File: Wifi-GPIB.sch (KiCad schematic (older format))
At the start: 18 parts

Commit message: Started dividing subsheets and sorted out power circuits. Active switching on USB/DC connector 5V.
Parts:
- removed CON?: POWER_BARREL, symbol BARREL_JACK
- removed U?: MICRO-B_USB, symbol MICRO-B_USB
- removed U?: BA33BC0FP-E2, TO-252, symbol BA33BC0FP-E2
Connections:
- wire segments 18 -> 19
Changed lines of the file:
@@
 LIBS:esp8266
 LIBS:ba33bc0fp-e2
+LIBS:ap1117e50g-13
+LIBS:irlml2246tr
 LIBS:Wifi-GPIB-cache
 EELAYER 25 0
@@
 $Descr A4 11693 8268
 encoding utf-8
-Sheet 1 1
+Sheet 1 2
 Title ""
 Date ""
@@
 $EndComp
 $Comp
-L BARREL_JACK CON?
-U 1 1 5564DEB5
-P 1250 1000
-F 0 "CON?" H 1250 1250 60  0000 C CNN
-F 1 "POWER_BARREL" H 1250 800 60  0000 C CNN
-F 2 "" H 1250 1000 60  0000 C CNN
-F 3 "" H 1250 1000 60  0000 C CNN
-	1    1250 1000
-	1    0    0    -1
-$EndComp
-$Comp
-L MICRO-B_USB U?
-U 1 1 5564E0EA
-P 1250 1900
-F 0 "U?" H 1250 1600 50  0000 C CNN
-F 1 "MICRO-B_USB" H 1250 2200 50  0000 C CNN
-F 2 "" H 1250 1900 60  0000 C CNN
-F 3 "" H 1250 1900 60  0000 C CNN
-	1    1250 1900
-	1    0    0    -1
-$EndComp
-$Comp
 L ESP-12/07v2/08v2 U?
 U 1 1 5564D82B
@@
 F 3 "" H 7850 1650 60  0000 C CNN
 	1    7850 1650
-	1    0    0    -1
-$EndComp
-$Comp
-L BA33BC0FP-E2 U?
-U 1 1 5564E643
-P 2850 950
-F 0 "U?" H 2650 1150 40  0000 C CNN
-F 1 "BA33BC0FP-E2" H 2850 1150 40  0000 L CNN
-F 2 "TO-252" H 2850 1050 30  0000 C CIN
-F 3 "" H 2850 950 60  0000 C CNN
-	1    2850 950
 	1    0    0    -1
 $EndComp
@@
 	10150 1850 10150 1900
 Wire Wire Line
-	9950 2400 10400 2400
+	9950 2400 10150 2400
+Wire Wire Line
+	10150 2400 10400 2400
 Wire Wire Line
 	11000 2400 11000 2550
@@
 Text GLabel 9050 1400 2    39   Input ~ 0
 ESP_TX
+$Sheet
+S 5100 7050 1700 600
+U 5565FD51
+F0 "Power Circuitry" 60
+F1 "power.sch" 60
+$EndSheet
 $EndSCHEMATC

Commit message: Update main sch to reference heirarchy. Add some more stuff to ESP.
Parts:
- removed D?: LED_DATA, symbol LED
- removed D?: LED_POWER, symbol LED
- removed JP?: ESP_FLASH_JUMP, symbol JUMPER
- removed P?: CONN_CENTRONICS_24, symbol CONN_CENTRONICS_24
- removed P?: CONN_4, symbol CONN_4
- removed R?: R, symbol R
- removed SW?: SW_RESET, symbol SW_PUSH
- removed U?: STM32F030C6, LQFP48, symbol STM32F030C6
- removed U?: SN75160B, MODULE, symbol SN75160B
- removed U?: SN75162B, MODULE, symbol SN75162B
- removed U?: ESP-12/07v2/08v2, symbol ESP-12/07v2/08v2
- removed W? (x2): TEST_GND, symbol TEST
- removed W?: TEST_3.3, symbol TEST
- removed W?: TEST_VIN, symbol TEST
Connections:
- net labels removed: +3.3V, ESP_GPIO0, ESP_RX, ESP_TX, GND, RESET
- wire segments 19 -> 0
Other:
- note removed: "ESP8266 Wifi Module"

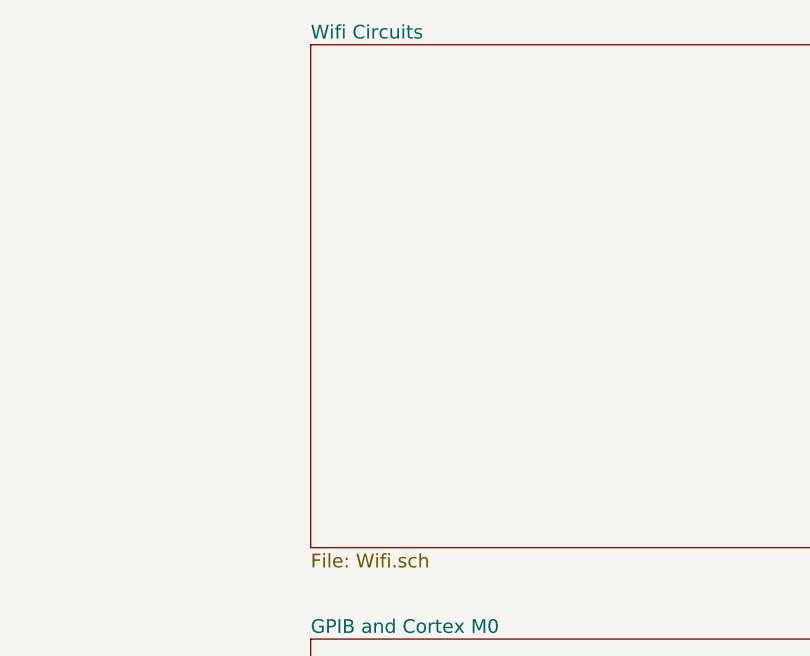
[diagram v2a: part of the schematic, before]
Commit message: Add testpoints and tidy up
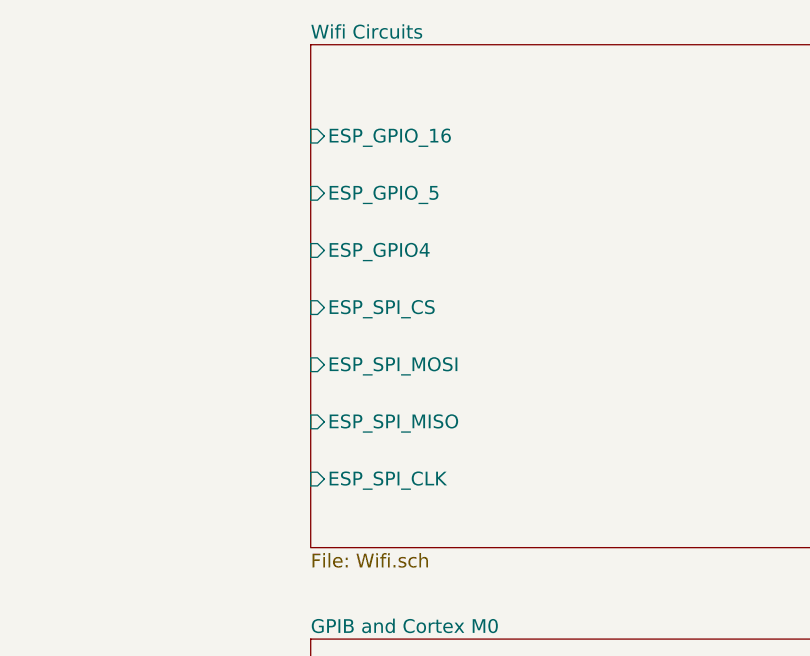
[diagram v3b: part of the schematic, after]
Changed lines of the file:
@@
 LIBS:ap1117e50g-13
 LIBS:irlml2246tr
+LIBS:testpoint
 LIBS:Wifi-GPIB-cache
 EELAYER 25 0
@@
 F0 "Wifi Circuits" 60
 F1 "Wifi.sch" 60
+F2 "ESP_SPI_CLK" I L 7050 3200 60
+F3 "ESP_SPI_MISO" I L 7050 2950 60
+F4 "ESP_SPI_MOSI" I L 7050 2700 60
+F5 "ESP_SPI_CS" I L 7050 2450 60
+F6 "ESP_GPIO4" I L 7050 2200 60
+F7 "ESP_GPIO_5" I L 7050 1950 60
+F8 "ESP_GPIO_16" I L 7050 1700 60
 $EndSheet
 $EndSCHEMATC

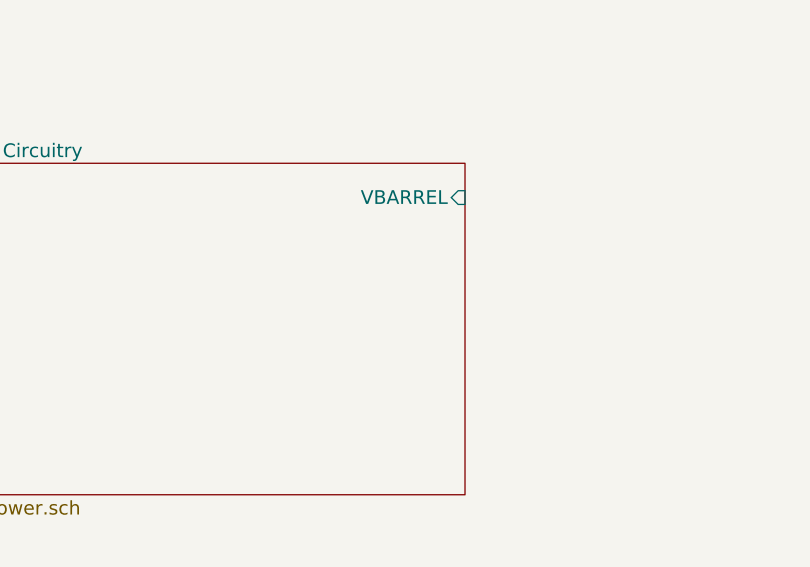
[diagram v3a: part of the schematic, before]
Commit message: More cleanup and swap out M0 model
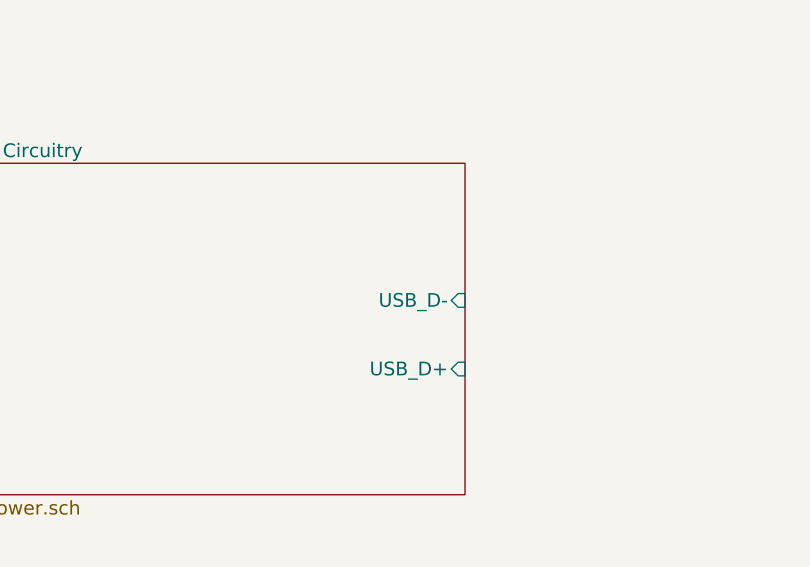
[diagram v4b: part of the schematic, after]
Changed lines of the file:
@@
 LIBS:irlml2246tr
 LIBS:testpoint
+LIBS:vin
+LIBS:stm32f072cbt6
 LIBS:Wifi-GPIB-cache
 EELAYER 25 0
@@
 F0 "Power Circuitry" 60
 F1 "power.sch" 60
-F2 "VBARREL" I R 3700 3050 60
+F3 "USB_D-" I R 3700 3500 60
+F4 "USB_D+" I R 3700 3800 60
 $EndSheet
 $Sheet

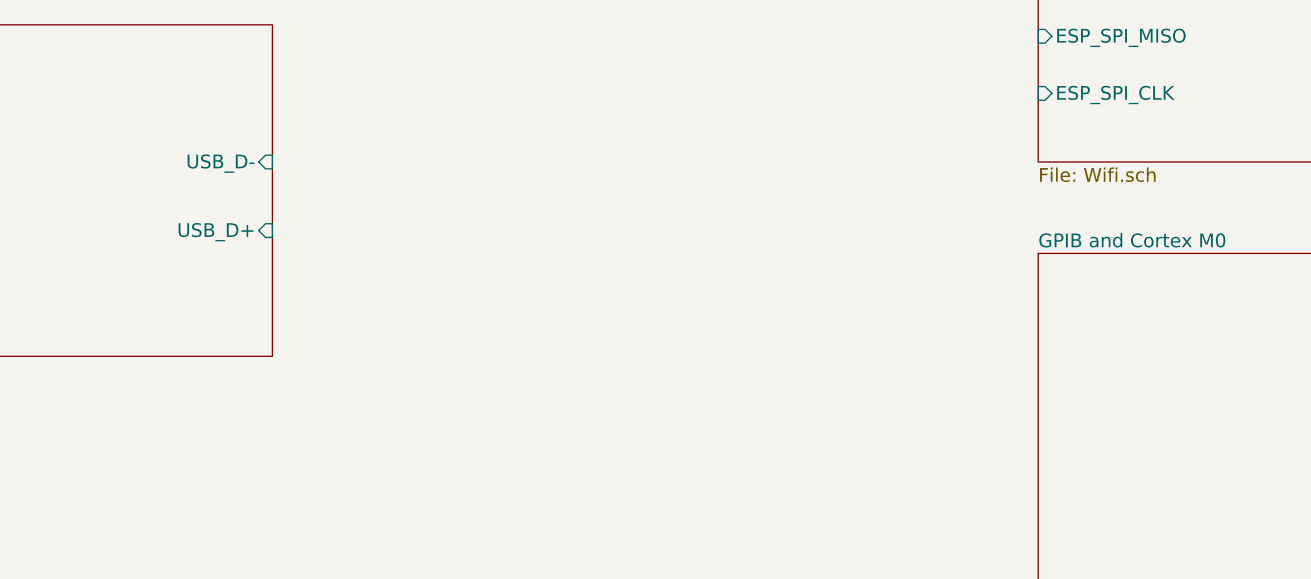
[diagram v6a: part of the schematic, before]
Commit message: Connect up USB pins
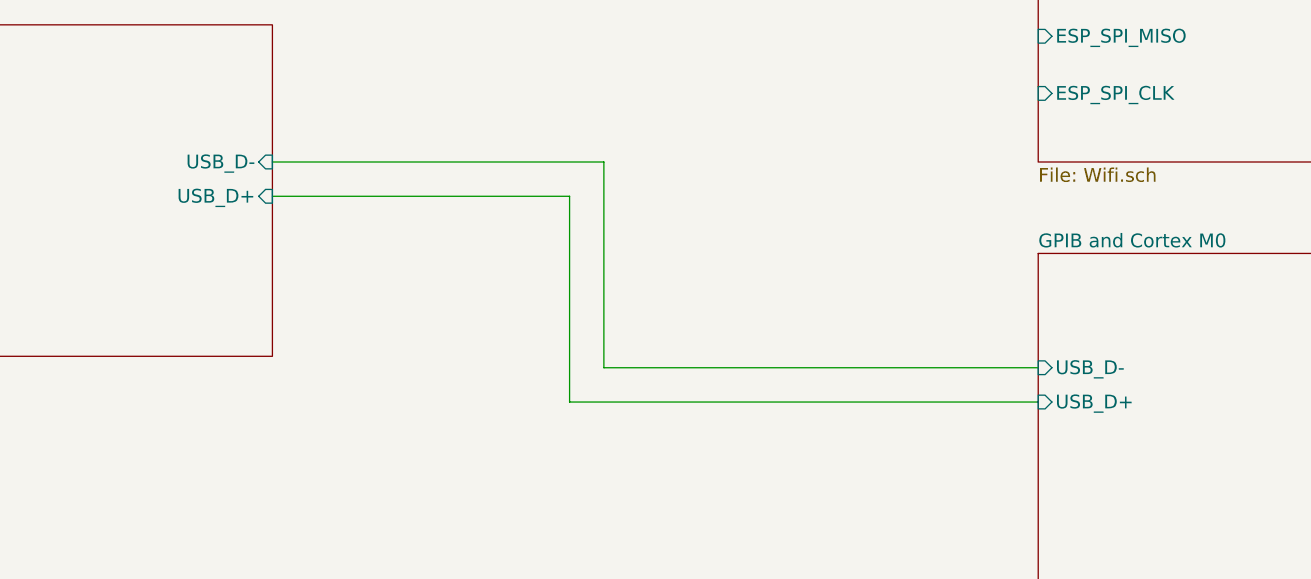
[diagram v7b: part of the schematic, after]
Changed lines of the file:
@@
 F1 "power.sch" 60
 F3 "USB_D-" I R 3700 3500 60
-F4 "USB_D+" I R 3700 3800 60
+F4 "USB_D+" I R 3700 3650 60
 $EndSheet
 $Sheet
@@
 F0 "GPIB and Cortex M0" 60
 F1 "GPIB.sch" 60
+F2 "USB_D-" I L 7050 4400 60
+F3 "USB_D+" I L 7050 4550 60
 $EndSheet
 $Sheet
@@
 F8 "ESP_GPIO_16" I L 7050 1700 60
 $EndSheet
+Wire Wire Line
+	3700 3500 5150 3500
+Wire Wire Line
+	5150 3500 5150 4400
+Wire Wire Line
+	5150 4400 7050 4400
+Wire Wire Line
+	3700 3650 5000 3650
+Wire Wire Line
+	5000 3650 5000 4550
+Wire Wire Line
+	5000 4550 7050 4550
 $EndSCHEMATC

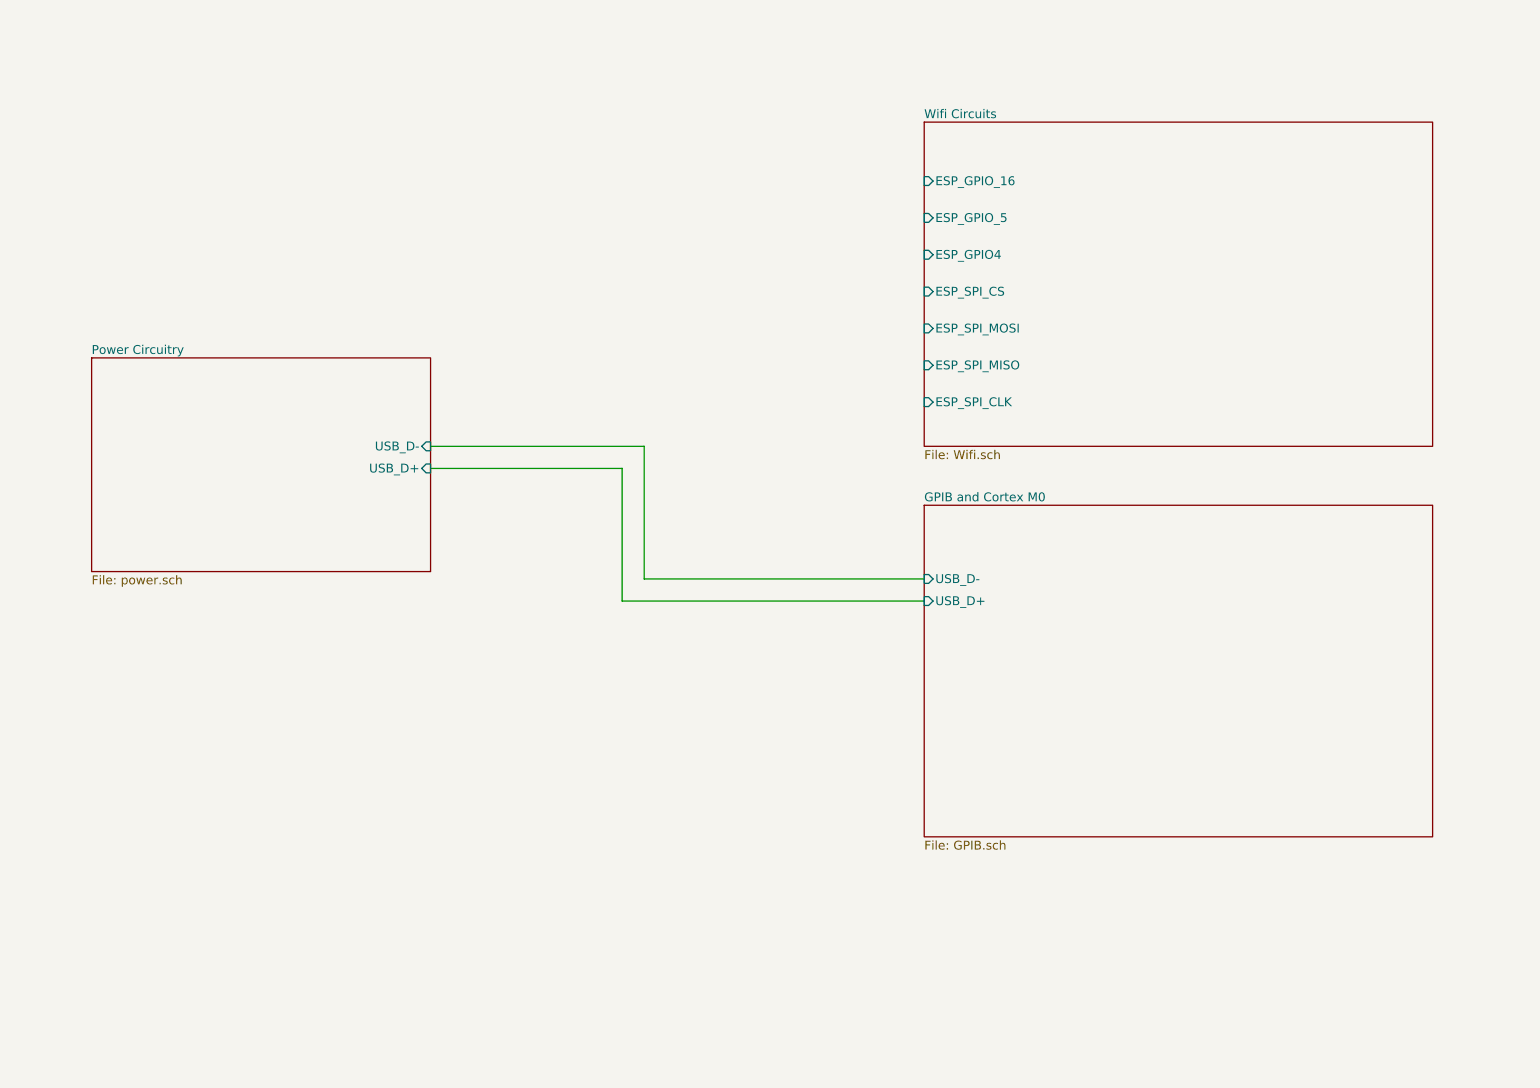
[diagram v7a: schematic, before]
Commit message: initial GPIB pin mappings
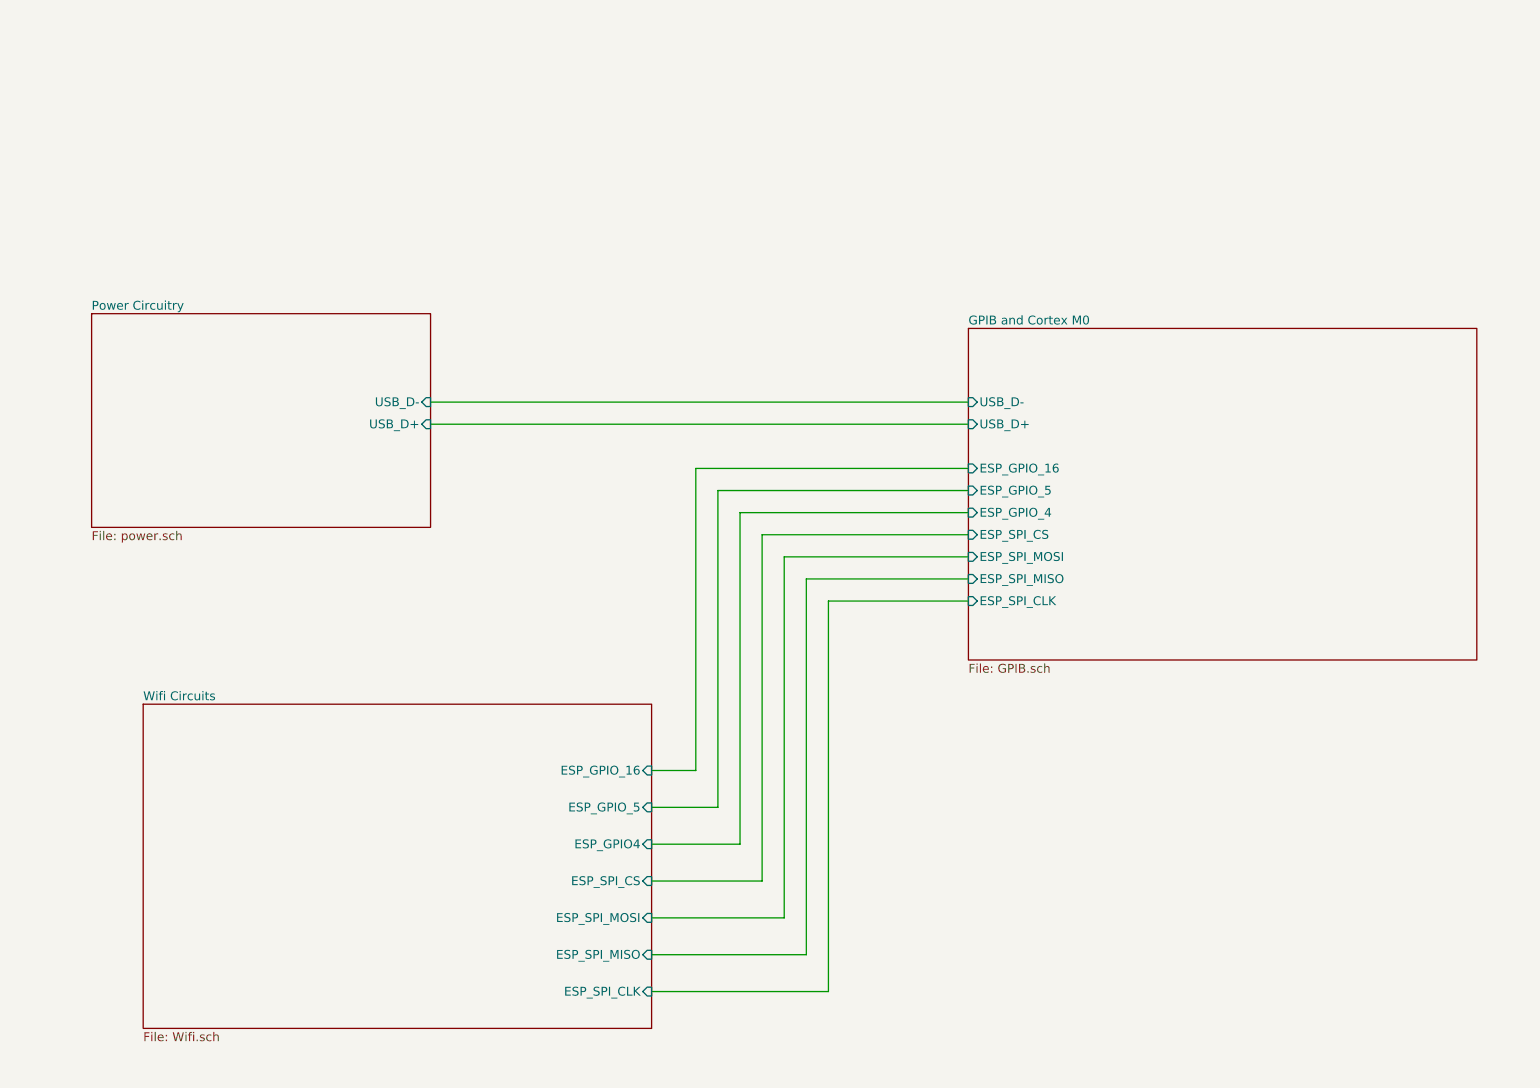
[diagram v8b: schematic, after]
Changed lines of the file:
@@
 $EndDescr
 $Sheet
-S 1400 2900 2300 1450
+S 1400 2600 2300 1450
 U 5565FD51
 F0 "Power Circuitry" 60
 F1 "power.sch" 60
-F3 "USB_D-" I R 3700 3500 60
-F4 "USB_D+" I R 3700 3650 60
+F3 "USB_D-" I R 3700 3200 60
+F4 "USB_D+" I R 3700 3350 60
 $EndSheet
 $Sheet
-S 7050 3900 3450 2250
+S 7350 2700 3450 2250
 U 55667032
 F0 "GPIB and Cortex M0" 60
 F1 "GPIB.sch" 60
-F2 "USB_D-" I L 7050 4400 60
-F3 "USB_D+" I L 7050 4550 60
+F2 "USB_D-" I L 7350 3200 60
+F3 "USB_D+" I L 7350 3350 60
+F4 "ESP_SPI_CS" I L 7350 4100 60
+F5 "ESP_SPI_MOSI" I L 7350 4250 60
+F6 "ESP_SPI_MISO" I L 7350 4400 60
+F7 "ESP_SPI_CLK" I L 7350 4550 60
+F8 "ESP_GPIO_16" I L 7350 3650 60
+F9 "ESP_GPIO_4" I L 7350 3950 60
+F10 "ESP_GPIO_5" I L 7350 3800 60
 $EndSheet
 $Sheet
-S 7050 1300 3450 2200
+S 1750 5250 3450 2200
 U 55667043
 F0 "Wifi Circuits" 60
 F1 "Wifi.sch" 60
-F2 "ESP_SPI_CLK" I L 7050 3200 60
-F3 "ESP_SPI_MISO" I L 7050 2950 60
-F4 "ESP_SPI_MOSI" I L 7050 2700 60
-F5 "ESP_SPI_CS" I L 7050 2450 60
-F6 "ESP_GPIO4" I L 7050 2200 60
-F7 "ESP_GPIO_5" I L 7050 1950 60
-F8 "ESP_GPIO_16" I L 7050 1700 60
+F2 "ESP_SPI_CLK" I R 5200 7200 60
+F3 "ESP_SPI_MISO" I R 5200 6950 60
+F4 "ESP_SPI_MOSI" I R 5200 6700 60
+F5 "ESP_SPI_CS" I R 5200 6450 60
+F6 "ESP_GPIO4" I R 5200 6200 60
+F7 "ESP_GPIO_5" I R 5200 5950 60
+F8 "ESP_GPIO_16" I R 5200 5700 60
 $EndSheet
 Wire Wire Line
-	3700 3500 5150 3500
+	3700 3200 7350 3200
 Wire Wire Line
-	5150 3500 5150 4400
+	3700 3350 7350 3350
 Wire Wire Line
-	5150 4400 7050 4400
+	5200 5700 5500 5700
 Wire Wire Line
-	3700 3650 5000 3650
+	5500 5700 5500 3650
 Wire Wire Line
-	5000 3650 5000 4550
+	5500 3650 7350 3650
 Wire Wire Line
-	5000 4550 7050 4550
+	5200 5950 5650 5950
+Wire Wire Line
+	5650 5950 5650 3800
+Wire Wire Line
+	5650 3800 7350 3800
+Wire Wire Line
+	5200 6200 5800 6200
+Wire Wire Line
+	5800 6200 5800 3950
+Wire Wire Line
+	5800 3950 7350 3950
+Wire Wire Line
+	5200 6450 5950 6450
+Wire Wire Line
+	5950 6450 5950 4100
+Wire Wire Line
+	5950 4100 7350 4100
+Wire Wire Line
+	5200 6700 6100 6700
+Wire Wire Line
+	6100 6700 6100 4250
+Wire Wire Line
+	6100 4250 7350 4250
+Wire Wire Line
+	5200 6950 6250 6950
+Wire Wire Line
+	6250 6950 6250 4400
+Wire Wire Line
+	6250 4400 7350 4400
+Wire Wire Line
+	5200 7200 6400 7200
+Wire Wire Line
+	6400 7200 6400 4550
+Wire Wire Line
+	6400 4550 7350 4550
 $EndSCHEMATC
